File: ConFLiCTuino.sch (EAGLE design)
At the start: 67 parts, among them IC1 MEGAARDUINO_CUSTOM, IC4 LM358D, Q1 IRLR024N, Q2 BC847B, Q3 BC847B, Q5 IRLR024N, Q6 IRLR024N, Q7 IRF9Z34NS, Q8 IRF9Z34NS

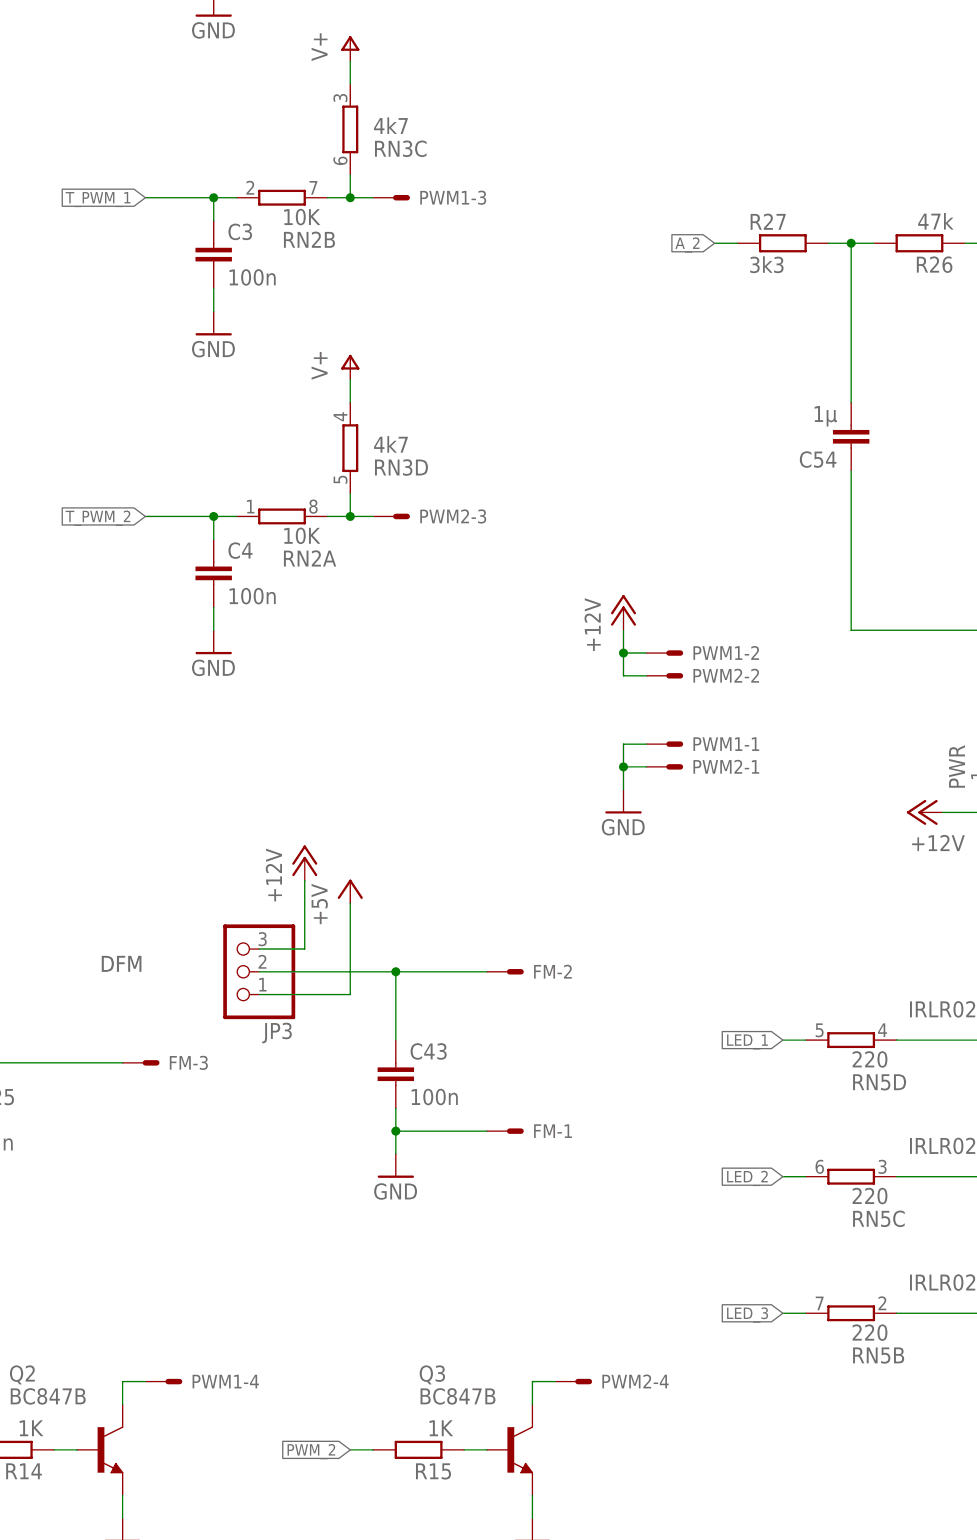
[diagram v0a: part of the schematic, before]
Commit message: init V0.6
Changed 4-Pol PWM connectors to Molex-Footprint with hole for the kex
pin.
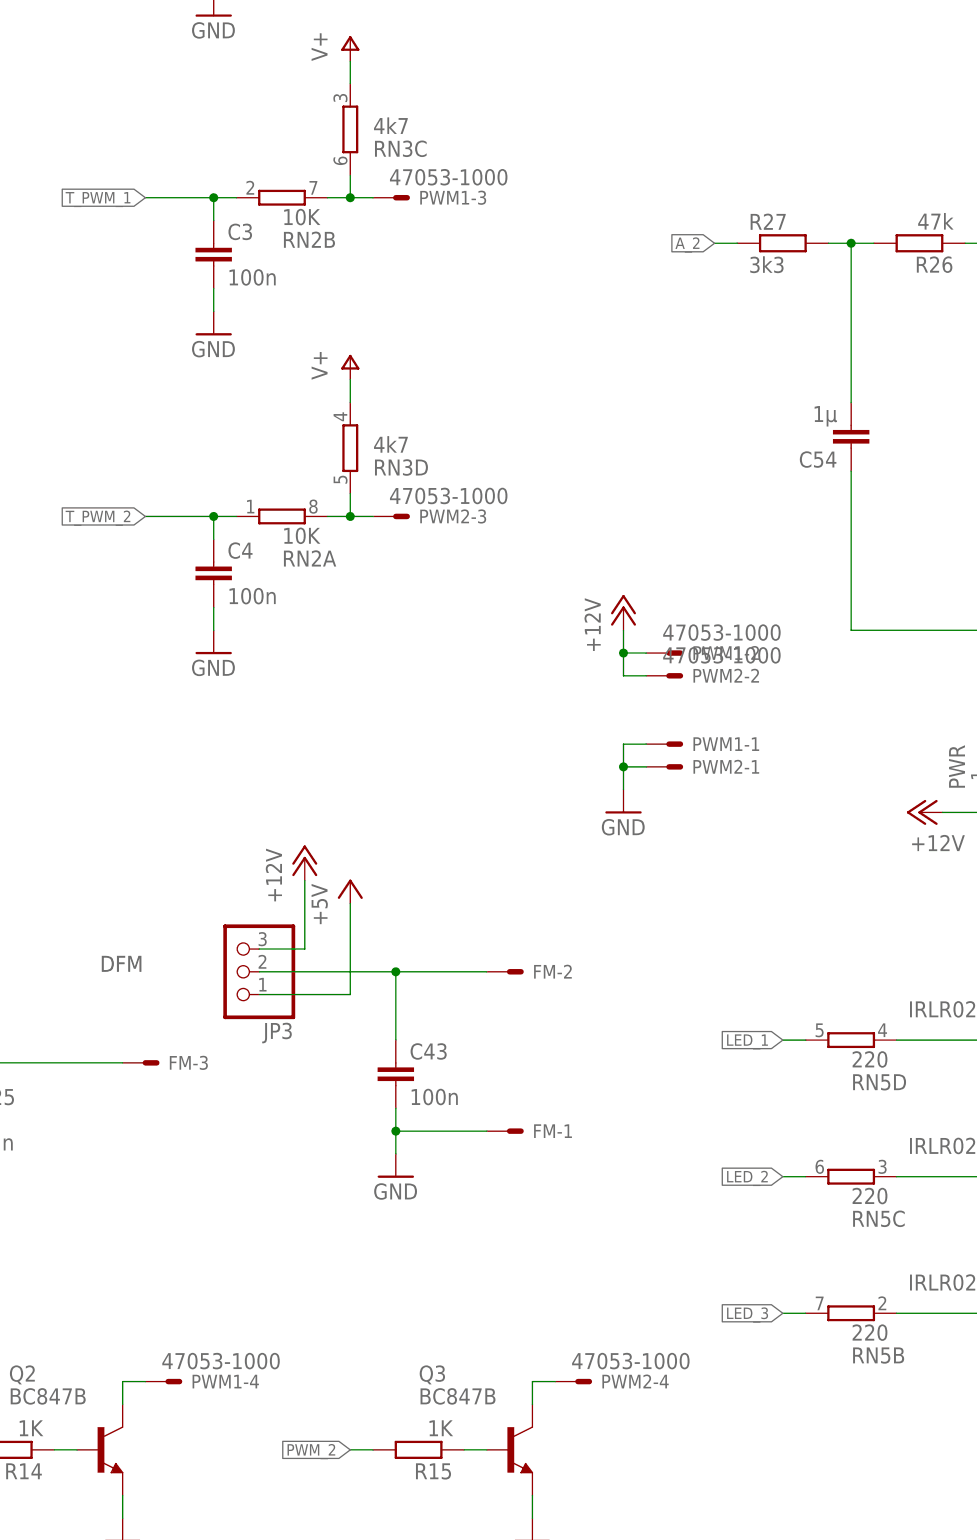
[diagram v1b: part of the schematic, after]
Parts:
- PWM1, PWM2: value 22-27-2041-04 -> 47053-1000; device con-molex:22-27-2041-04 -> con-molex:47053-1000
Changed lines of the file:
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@@
 <part name="R27" library="rcl" deviceset="R-EU_" device="M0805" value="3k3"/>
 <part name="C54" library="rcl" deviceset="C-EU" device="C0805K" value="1µ"/>
-<part name="PWM1" library="con-molex" deviceset="22-?-04" device="27-2041"/>
-<part name="PWM2" library="con-molex" deviceset="22-?-04" device="27-2041"/>
+<part name="PWM1" library="con-molex" deviceset="47053-1000" device=""/>
+<part name="PWM2" library="con-molex" deviceset="47053-1000" device=""/>
 <part name="R14" library="rcl" deviceset="R-EU_" device="M0805" value="1K"/>
 <part name="P+1" library="supply1" deviceset="+12V" device=""/>
